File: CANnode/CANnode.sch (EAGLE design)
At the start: 247 parts, among them IC1 ISO1050DUB, IC2 ISO1050DUB, Q1 FDV302P, Q3 FDV302P, U1 LM324PW, U10 FT2232HL, U11 93LC56C-I/SN, U2 TPS70445_PWP_24, U3 LM324PW, U4 LM324PW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

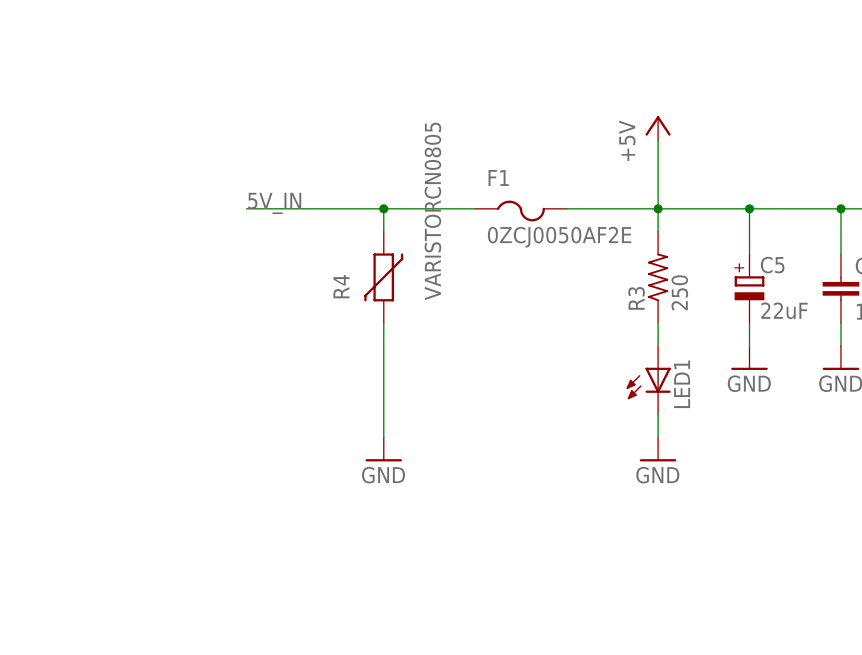
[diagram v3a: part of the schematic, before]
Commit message: Updated input protection.
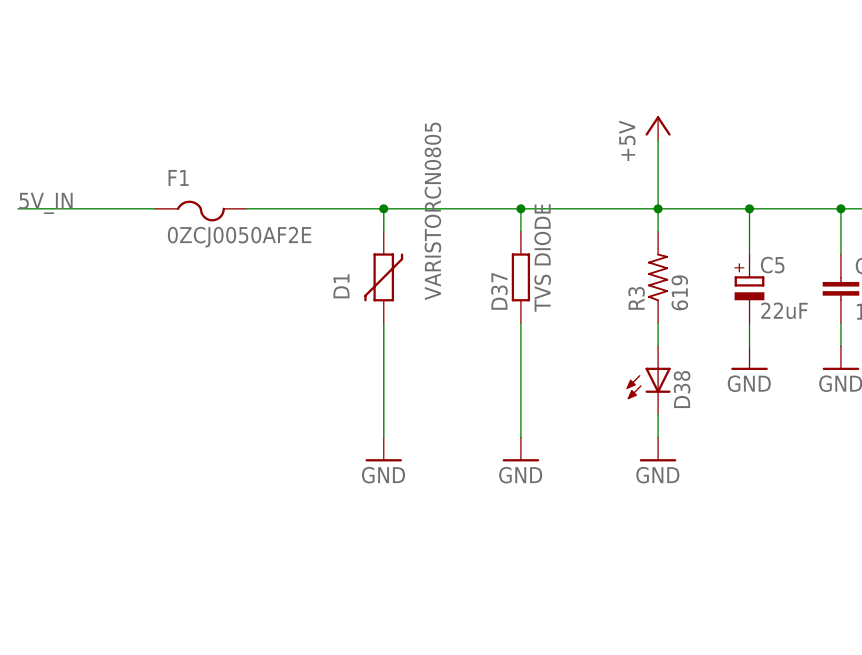
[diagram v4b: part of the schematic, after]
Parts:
- added D37: TVS DIODE, eagle-ltspice:RR0402
- R3: value 250 -> 619
- renumbered LED1 to D38, R4 to D1
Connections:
- net +5V: now also D1.1, D37.2
- net 5V_IN: no longer D1.1
- net GND: now also D37.1
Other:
- moved on the sheet: F1
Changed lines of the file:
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@@
 <part name="+3V1" library="supply1" deviceset="+3V3" device=""/>
 <part name="U$1" library="supply1" deviceset="+1V2" device=""/>
-<part name="R3" library="resistor" deviceset="R-US_" device="R0402" value="250"/>
-<part name="LED1" library="led" deviceset="LED" device=""/>
-<part name="R4" library="varistor" deviceset="VARISTOR" device="CN0805"/>
+<part name="R3" library="resistor" deviceset="R-US_" device="R0402" value="619"/>
+<part name="D38" library="led" deviceset="LED" device=""/>
+<part name="D1" library="varistor" deviceset="VARISTOR" device="CN0805"/>
 <part name="R5" library="resistor" deviceset="R-US_" device="R0402" value="DNP"/>
 <part name="R6" library="resistor" deviceset="R-US_" device="R0402" value="DNP"/>
@@
 <part name="GND130" library="supply1" deviceset="GND" device=""/>
 <part name="D36" library="zetex" deviceset="D" device="SOD323"/>
+<part name="D37" library="eagle-ltspice" deviceset="R" device="R0402" value="TVS DIODE"/>
+<part name="GND131" library="supply1" deviceset="GND" device=""/>
 </parts>
 <sheets>
@@
 <instance part="U$1" gate="A" x="248.92" y="2.54"/>
 <instance part="R3" gate="G$1" x="30.48" y="5.08" rot="R90"/>
-<instance part="LED1" gate="G$1" x="30.48" y="-5.08"/>
-<instance part="R4" gate="G$1" x="0" y="5.08" rot="R90"/>
+<instance part="D38" gate="G$1" x="30.48" y="-5.08"/>
+<instance part="D1" gate="G$1" x="0" y="5.08" rot="R90"/>
 <instance part="R5" gate="G$1" x="523.24" y="25.4" rot="R90"/>
 <instance part="R6" gate="G$1" x="520.7" y="-48.26" rot="R90"/>
@@
 <instance part="C74" gate="G$1" x="58.42" y="5.08"/>
 <instance part="GND123" gate="1" x="58.42" y="-5.08"/>
-<instance part="F1" gate="G$1" x="15.24" y="10.16"/>
+<instance part="F1" gate="G$1" x="-20.32" y="10.16"/>
 <instance part="X2" gate="-1" x="182.88" y="-137.16"/>
 <instance part="X2" gate="-2" x="182.88" y="-144.78"/>
@@
 <instance part="GND130" gate="1" x="93.98" y="15.24"/>
 <instance part="D36" gate="G$1" x="78.74" y="-33.02" rot="R180"/>
+<instance part="D37" gate="G$1" x="15.24" y="5.08" rot="R90"/>
+<instance part="GND131" gate="1" x="15.24" y="-15.24"/>
 </instances>
 <busses>
@@
 <net name="N$2" class="0">
 <segment>
-<pinref part="LED1" gate="G$1" pin="A"/>
+<pinref part="D38" gate="G$1" pin="A"/>
 <pinref part="R3" gate="G$1" pin="1"/>
 <wire x1="30.48" y1="-2.54" x2="30.48" y2="0" width="0.1524" layer="91"/>
@@
 </segment>
 <segment>
-<pinref part="R4" gate="G$1" pin="2"/>
+<pinref part="D1" gate="G$1" pin="2"/>
 <wire x1="0" y1="0" x2="0" y2="-12.7" width="0.1524" layer="91"/>
 <pinref part="GND5" gate="1" pin="GND"/>
 </segment>
 <segment>
-<pinref part="LED1" gate="G$1" pin="C"/>
+<pinref part="D38" gate="G$1" pin="C"/>
 <wire x1="30.48" y1="-12.7" x2="30.48" y2="-10.16" width="0.1524" layer="91"/>
 <pinref part="GND6" gate="1" pin="GND"/>
@@
 <pinref part="GND125" gate="1" pin="GND"/>
 </segment>
+<segment>
+<pinref part="GND131" gate="1" pin="GND"/>
+<pinref part="D37" gate="G$1" pin="1"/>
+<wire x1="15.24" y1="-12.7" x2="15.24" y2="0" width="0.1524" layer="91"/>
+</segment>
 </net>
 <net name="A0_BUFFERED" class="0">
@@
 </segment>
 <segment>
-<wire x1="10.16" y1="12.7" x2="0" y2="12.7" width="0.1524" layer="91"/>
-<pinref part="R4" gate="G$1" pin="1"/>
-<wire x1="0" y1="10.16" x2="0" y2="12.7" width="0.1524" layer="91"/>
-<junction x="0" y="12.7"/>
-<wire x1="0" y1="12.7" x2="-15.24" y2="12.7" width="0.1524" layer="91"/>
-<label x="-15.24" y="12.7" size="1.778" layer="95"/>
-<pinref part="F1" gate="G$1" pin="1"/>
-</segment>
-<segment>
 <pinref part="U$5" gate="G$1" pin="VBUS"/>
 <wire x1="-2.54" y1="-78.74" x2="7.62" y2="-78.74" width="0.1524" layer="91"/>
@@
 <label x="167.64" y="-182.88" size="1.778" layer="95"/>
 </segment>
+<segment>
+<pinref part="F1" gate="G$1" pin="1"/>
+<wire x1="-25.4" y1="12.7" x2="-40.64" y2="12.7" width="0.1524" layer="91"/>
+<label x="-40.64" y="12.7" size="1.778" layer="95"/>
+</segment>
 </net>
 <net name="N$20" class="0">
@@
 <wire x1="50.8" y1="12.7" x2="40.64" y2="12.7" width="0.1524" layer="91"/>
 <wire x1="40.64" y1="12.7" x2="30.48" y2="12.7" width="0.1524" layer="91"/>
-<wire x1="30.48" y1="12.7" x2="20.32" y2="12.7" width="0.1524" layer="91"/>
 <wire x1="30.48" y1="10.16" x2="30.48" y2="12.7" width="0.1524" layer="91"/>
 <junction x="30.48" y="12.7"/>
@@
 <junction x="58.42" y="12.7"/>
 <pinref part="F1" gate="G$1" pin="2"/>
+<wire x1="-15.24" y1="12.7" x2="0" y2="12.7" width="0.1524" layer="91"/>
+<pinref part="D1" gate="G$1" pin="1"/>
+<wire x1="0" y1="12.7" x2="15.24" y2="12.7" width="0.1524" layer="91"/>
+<wire x1="15.24" y1="12.7" x2="30.48" y2="12.7" width="0.1524" layer="91"/>
+<wire x1="0" y1="10.16" x2="0" y2="12.7" width="0.1524" layer="91"/>
+<junction x="0" y="12.7"/>
+<pinref part="D37" gate="G$1" pin="2"/>
+<wire x1="15.24" y1="10.16" x2="15.24" y2="12.7" width="0.1524" layer="91"/>
+<junction x="15.24" y="12.7"/>
 </segment>
 <segment>

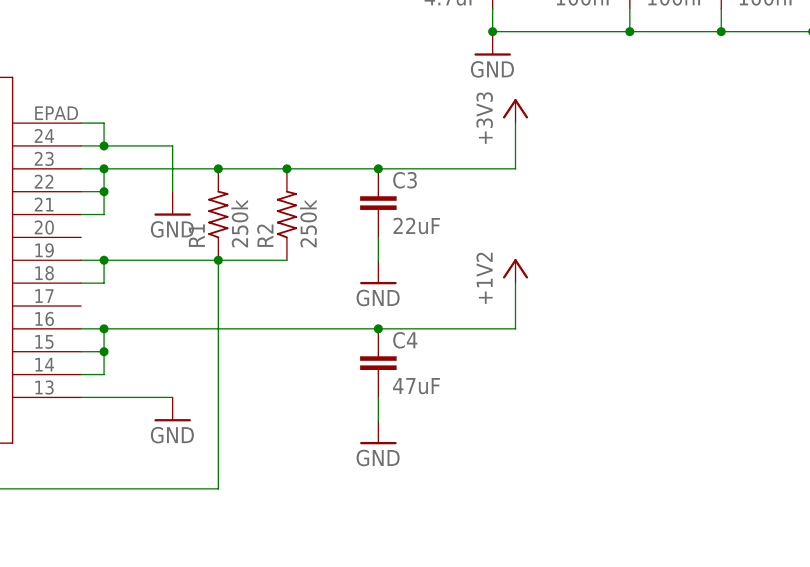
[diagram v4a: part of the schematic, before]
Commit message: changed power caps to 0805. working on BOM
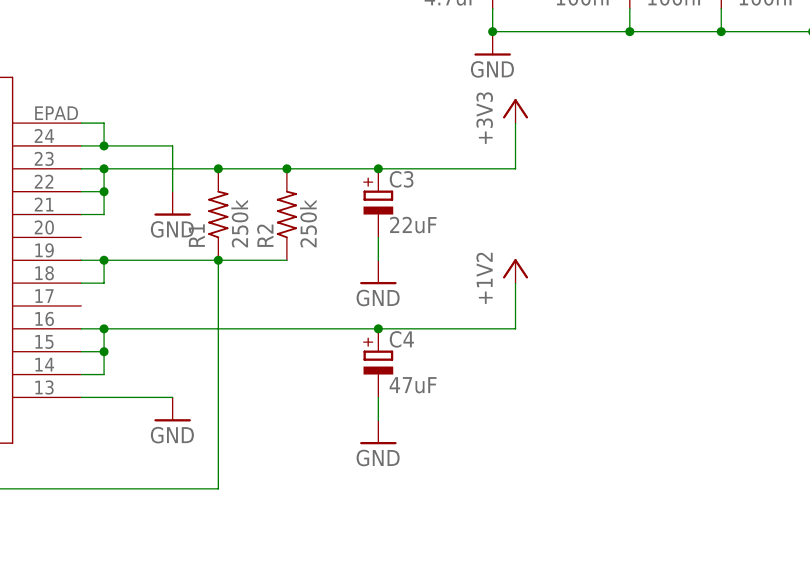
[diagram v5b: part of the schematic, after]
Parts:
- C3, C4: device eagle-ltspice:CC0402 -> resistor:CPOL-EUCT3528
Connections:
- net +1V2: now also C4.+; no longer C4.1
- net +3V3: now also C3.+; no longer C3.1
- net GND: now also C3.-, C4.-; no longer C3.2, C4.2
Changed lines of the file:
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@@
 <?xml version="1.0" encoding="utf-8"?>
 <!DOCTYPE eagle SYSTEM "eagle.dtd">
-<eagle version="7.5.0">
+<eagle version="6.6.0">
 <drawing>
 <settings>
@@
 <part name="R1" library="resistor" deviceset="R-US_" device="R0402" value="250k"/>
 <part name="R2" library="resistor" deviceset="R-US_" device="R0402" value="250k"/>
-<part name="C3" library="eagle-ltspice" deviceset="C" device="C0402" value="22uF"/>
-<part name="C4" library="eagle-ltspice" deviceset="C" device="C0402" value="47uF"/>
 <part name="+3V1" library="supply1" deviceset="+3V3" device=""/>
 <part name="U$1" library="supply1" deviceset="+1V2" device=""/>
@@
 <part name="D37" library="eagle-ltspice" deviceset="R" device="R0402" value="TVS DIODE"/>
 <part name="GND131" library="supply1" deviceset="GND" device=""/>
+<part name="C3" library="resistor" deviceset="CPOL-EU" device="CT3528" value="22uF"/>
+<part name="C4" library="resistor" deviceset="CPOL-EU" device="CT3528" value="47uF"/>
 </parts>
 <sheets>
@@
 <instance part="R1" gate="G$1" x="215.9" y="7.62" rot="R90"/>
 <instance part="R2" gate="G$1" x="223.52" y="7.62" rot="R90"/>
-<instance part="C3" gate="G$1" x="233.68" y="10.16"/>
-<instance part="C4" gate="G$1" x="233.68" y="-7.62"/>
 <instance part="+3V1" gate="G$1" x="248.92" y="20.32"/>
 <instance part="U$1" gate="A" x="248.92" y="2.54"/>
@@
 <instance part="D37" gate="G$1" x="15.24" y="5.08" rot="R90"/>
 <instance part="GND131" gate="1" x="15.24" y="-15.24"/>
+<instance part="C3" gate="G$1" x="233.68" y="10.16"/>
+<instance part="C4" gate="G$1" x="233.68" y="-7.62"/>
 </instances>
 <busses>
@@
 <pinref part="R2" gate="G$1" pin="2"/>
 <junction x="223.52" y="12.7"/>
+<pinref part="+3V1" gate="G$1" pin="+3V3"/>
 <wire x1="223.52" y1="12.7" x2="233.68" y2="12.7" width="0.1524" layer="91"/>
-<pinref part="C3" gate="G$1" pin="1"/>
-<junction x="233.68" y="12.7"/>
-<pinref part="+3V1" gate="G$1" pin="+3V3"/>
 <wire x1="233.68" y1="12.7" x2="248.92" y2="12.7" width="0.1524" layer="91"/>
 <wire x1="248.92" y1="12.7" x2="248.92" y2="17.78" width="0.1524" layer="91"/>
+<pinref part="C3" gate="G$1" pin="+"/>
+<junction x="233.68" y="12.7"/>
 </segment>
 <segment>
@@
 <wire x1="203.2" y1="-5.08" x2="233.68" y2="-5.08" width="0.1524" layer="91"/>
 <junction x="203.2" y="-5.08"/>
-<pinref part="C4" gate="G$1" pin="1"/>
-<junction x="233.68" y="-5.08"/>
 <pinref part="U$1" gate="A" pin="+1V2"/>
 <wire x1="233.68" y1="-5.08" x2="248.92" y2="-5.08" width="0.1524" layer="91"/>
 <wire x1="248.92" y1="-5.08" x2="248.92" y2="0" width="0.1524" layer="91"/>
+<pinref part="C4" gate="G$1" pin="+"/>
+<junction x="233.68" y="-5.08"/>
 </segment>
 <segment>
@@
 </segment>
 <segment>
-<pinref part="C3" gate="G$1" pin="2"/>
 <wire x1="233.68" y1="2.54" x2="233.68" y2="5.08" width="0.1524" layer="91"/>
 <pinref part="GND3" gate="1" pin="GND"/>
-</segment>
-<segment>
-<pinref part="C4" gate="G$1" pin="2"/>
+<pinref part="C3" gate="G$1" pin="-"/>
+</segment>
+<segment>
 <wire x1="233.68" y1="-15.24" x2="233.68" y2="-12.7" width="0.1524" layer="91"/>
 <pinref part="GND4" gate="1" pin="GND"/>
-</segment>
-<segment>
+<pinref part="C4" gate="G$1" pin="-"/>
+</segment>
+<segment>

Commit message: CAN resistors
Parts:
- R5, R6: value DNP -> 120
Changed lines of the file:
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@@
 <part name="D38" library="led" deviceset="LED" device=""/>
 <part name="D1" library="varistor" deviceset="VARISTOR" device="CN0805"/>
-<part name="R5" library="resistor" deviceset="R-US_" device="R0402" value="DNP"/>
-<part name="R6" library="resistor" deviceset="R-US_" device="R0402" value="DNP"/>
+<part name="R5" library="resistor" deviceset="R-US_" device="R0402" value="120"/>
+<part name="R6" library="resistor" deviceset="R-US_" device="R0402" value="120"/>
 <part name="C9" library="eagle-ltspice" deviceset="C" device="C0402" value=".1uF"/>
 <part name="C10" library="eagle-ltspice" deviceset="C" device="C0402" value=".1uF"/>
